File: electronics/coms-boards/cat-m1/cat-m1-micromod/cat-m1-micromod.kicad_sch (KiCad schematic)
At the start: 61 parts

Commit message: removed 3.3v to 1.8v reg from sara-m410m board and approved for pcb routing, added m.2 connector pcb for pycom boards under duel communications board
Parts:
- removed C? (x2): 1uF, symbol Device:C
- removed R?: 100K, symbol Device:R
- removed U?: AP7331-18WG-7, SOT95P285X145-5N, symbol AP7331-18WG-7:AP7331-18WG-7
- added TP?: VCC, symbol Connector:TestPoint
- R?: value 35K -> 10K
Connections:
- net VCC: now also TP?.1
- net GPIO_VCC_ON renamed GPIO_VCC_EN
- net GPIO_V_INT: no longer names the net of J?.57 (F5)
- no-connect marks 34 -> 62
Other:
- note added: "6th October 2022"
- note added: "CAT-M1 M.2 Card"
- note added: "LED Network Indicator"
- note added: "Level Shifter 3.3 V -> 1.8 V"
- note added: "MicroMod Connector"
- note added: "Nano Sim Connector"
- note added: "Reset Switch"
- note added: "USB-C Connector"
- note removed: "1.8 V Reference Voltage"
- note removed: "MQTT"
- note removed: "Note. EN1V8 should be pulled low before GPIO_VCC_ON is switched off."
- moved on the sheet: C?, D?, J?, L?, Q?, R?, U?

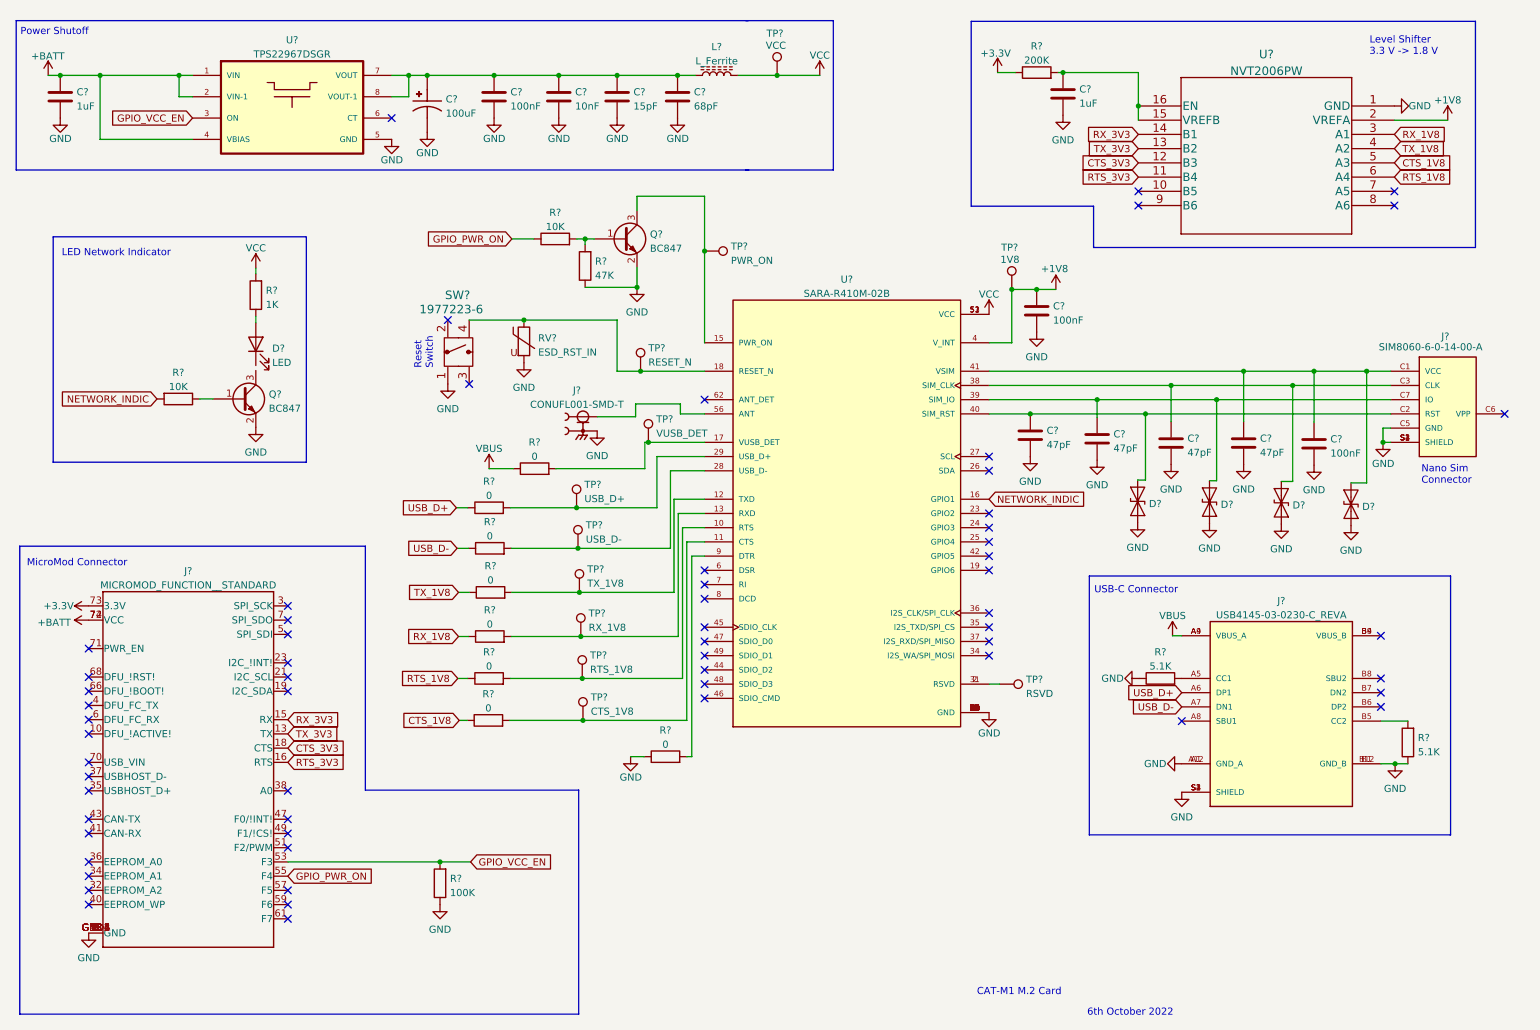
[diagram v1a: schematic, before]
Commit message: finalised cat-m1 m.2 connector board for communications
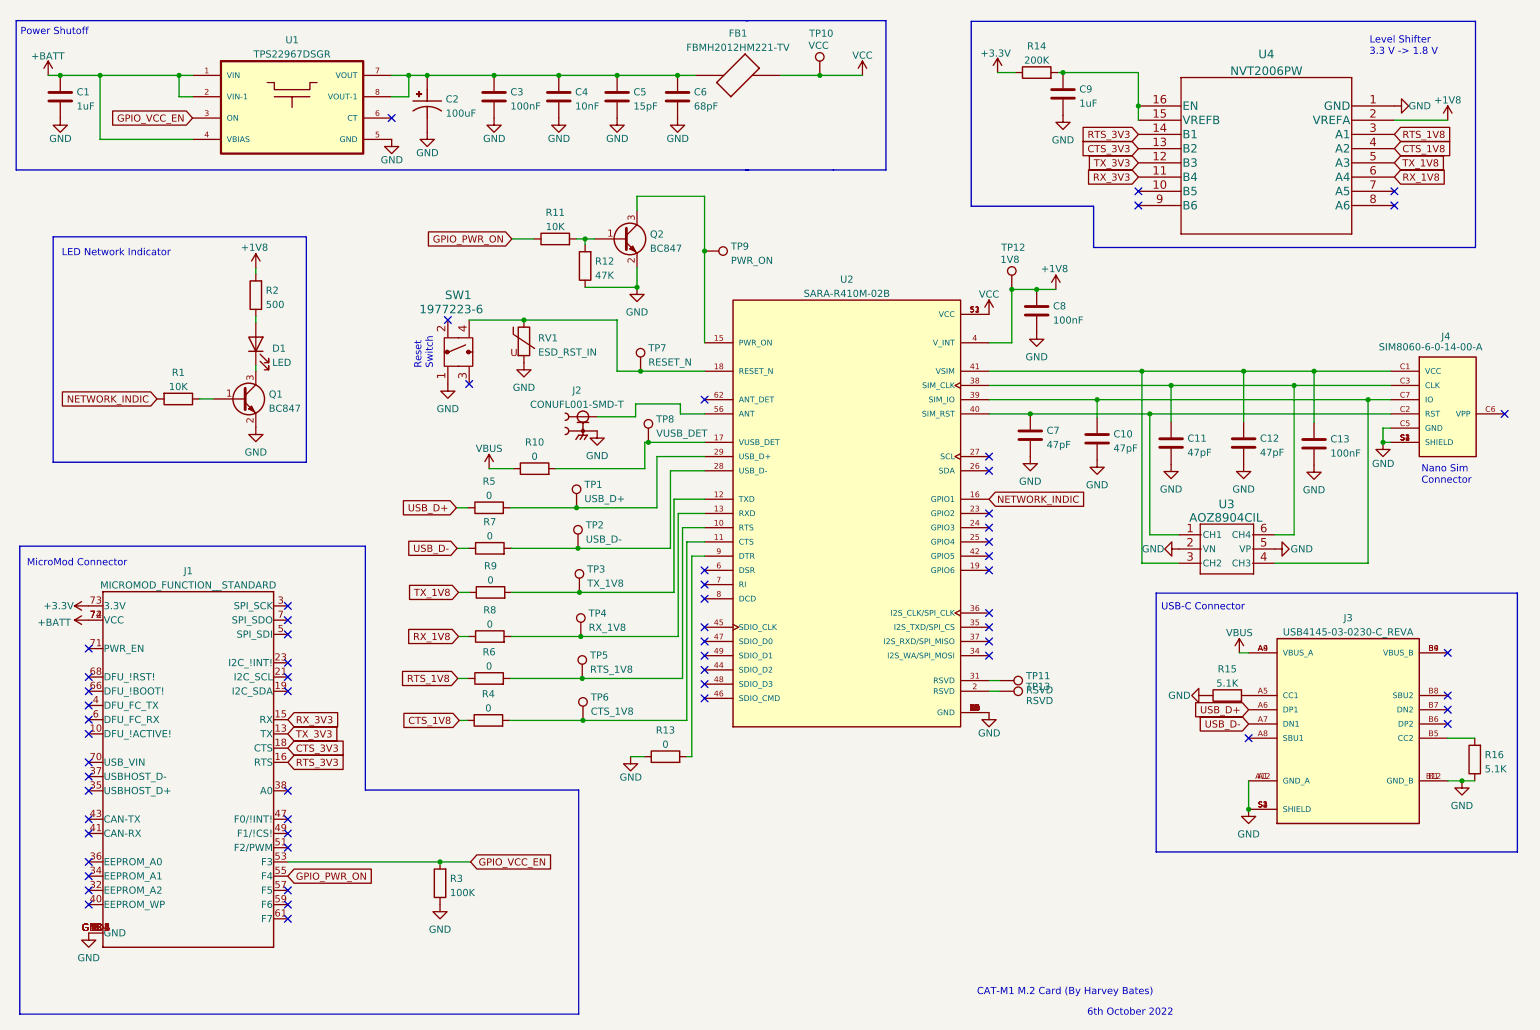
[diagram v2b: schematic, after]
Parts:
- removed D? (x4): PESD0402-140, symbol Diode:SD05_SOD323
- removed L?: L_Ferrite, symbol Device:L_Ferrite
- added FB1: FBMH2012HM221-TV, FBMH2012HM221-TV:BEADC2012X105N, symbol FBMH2012HM221-TV:FBMH2012HM221-TV
- added TP13: RSVD, TestPoint:TestPoint_Pad_D1.0mm, symbol Connector:TestPoint
- added U3: AOZ8904CIL, AOZ8904CIL:AOZ8904CIL, symbol AOZ8904CIL:AOZ8904CIL
- C1, C10, C11, C12, C13, C3, C4, C5, C6, C7, C8, C9: renamed from C?; footprint (none) -> Capacitor_SMD:C_0805_2012Metric
- C2: renamed from C?; footprint CAPPM3528X210N -> T520B107M006ATE015:CAPPM3528X210N
- D1: renamed from D?; footprint (none) -> Capacitor_SMD:C_0805_2012Metric
- J2: renamed from J?; footprint LINX_CONUFL001-SMD-T -> CONUFL001-SMD-T:LINX_CONUFL001-SMD-T
- J3: renamed from J?; footprint GCT_USB4145-03-0230-C_REVA -> USB4145-03-0230-C_REVA:GCT_USB4145-03-0230-C_REVA
- J4: renamed from J?; footprint GCT_SIM8060-6-0-14-00-A -> SIM8060-6-0-14-00-A:GCT_SIM8060-6-0-14-00-A
- R1, R10, R11, R12, R13, R14, R15, R16, R3, R4, R5, R6, R7, R8, R9: renamed from R?; footprint (none) -> Resistor_SMD:R_0805_2012Metric
- R2: renamed from R?; value 1K -> 500; footprint (none) -> Resistor_SMD:R_0805_2012Metric
- RV1: renamed from RV?; footprint (none) -> Resistor_SMD:R_0805_2012Metric; Component (none) -> VC080518A400DP
- SW1: renamed from SW?; footprint SW_1977223-6_TEC -> footprints:1977223-6
- TP1, TP10, TP11, TP12, TP2, TP3, TP4, TP5, TP6, TP7, TP8, TP9: renamed from TP?; footprint (none) -> TestPoint:TestPoint_Pad_D1.0mm
- U1: renamed from U?; footprint SON50P200X200X80-9N -> TPS22967DSGR:SON50P200X200X80-9N
- U2: renamed from U?; footprint XCVR_SARA-R410M-02B -> SARA-R410M-02B:XCVR_SARA-R410M-02B
- U4: renamed from U?; footprint TSSOP16_SOT403-1_NXP -> NVT2006PW:NVT2006PW
- gave numbers to parts that had none: 3
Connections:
- net +1V8: now also R2.2
- net CTS_1V8: now also U4.4 (A2); no longer U4.5 (A3)
- net CTS_3V3: now also U4.13 (B2); no longer U4.12 (B3)
- net GND: now also U3.2 (VN), U3.5 (VP)
- net RTS_1V8: now also U4.3 (A1); no longer U4.6 (A4)
- net RTS_3V3: now also U4.14 (B1); no longer U4.11 (B4)
- net RX_1V8: now also U4.6 (A4); no longer U4.3 (A1)
- net RX_3V3: now also U4.11 (B4); no longer U4.14 (B1)
- net TX_1V8: now also U4.5 (A3); no longer U4.4 (A2)
- net TX_3V3: now also U4.12 (B3); no longer U4.13 (B2)
- net VCC: now also FB1.2; no longer R2.2
- net at C12.1, C13.1, J4.C1 (VCC)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: now also U3.3 (CH2)
- net at C7.1, J4.C2 (RST), U2.40 (SIM_RST): now also U3.1 (CH1)
- net at C11.1, J4.C3 (CLK), U2.38 (SIM_CLK): now also U3.6 (CH4)
- net at C10.1, J4.C7 (IO), U2.39 (SIM_IO): now also U3.4 (CH3)
- net at Q1.3 (C): now also D1.1 (K)
- net at C2.1, C3.1, C4.1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: now also FB1.1
- net at TP11.1, U2.31 (RSVD): no longer U2.2 (RSVD)
- new net: TP13.1, U2.2 (RSVD)
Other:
- note added: "CAT-M1 M.2 Card (By Harvey Bates)"
- note removed: "CAT-M1 M.2 Card"
- moved on the sheet: J3, R15, R16, TP10, TP11

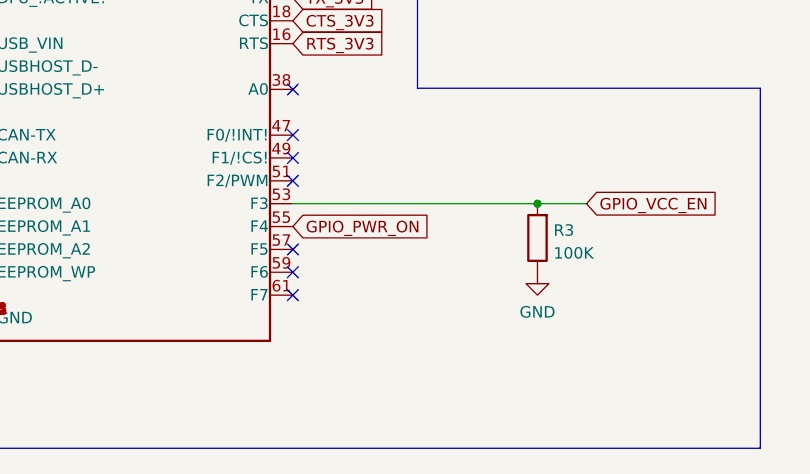
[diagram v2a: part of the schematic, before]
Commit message: updated to re-align with master
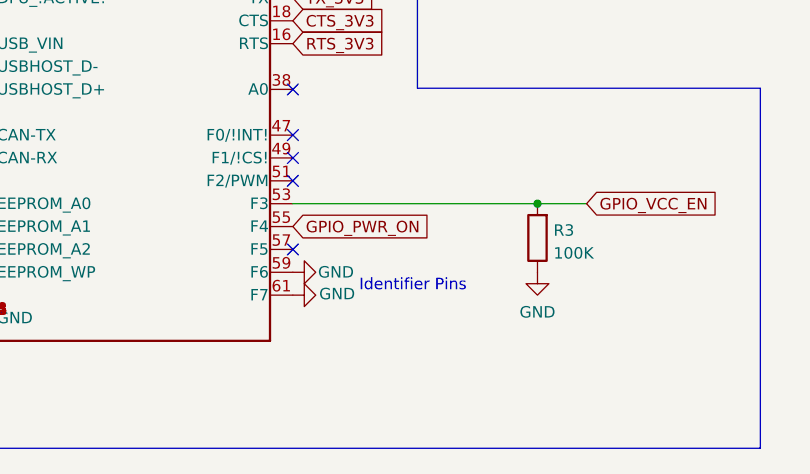
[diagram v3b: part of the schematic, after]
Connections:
- net GND: now also J1.59 (F6), J1.61 (F7)
- no-connect marks 62 -> 60
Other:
- note added: "Identifier Pins"
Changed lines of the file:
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@@
   (no_connect (at 28.321 133.604))
   (no_connect (at 63.881 161.544))
-  (no_connect (at 63.881 176.784))
   (no_connect (at 63.881 164.084))
   (no_connect (at 63.881 159.004))
@@
   (no_connect (at 189.103 129.794))
   (no_connect (at 281.178 86.614))
-  (no_connect (at 63.881 174.244))
   (no_connect (at 63.881 171.704))
   (no_connect (at 189.103 96.774))
@@
     (effects (font (size 1.27 1.27)) (justify left bottom))
   )
+  (text "Identifier Pins" (at 71.247 176.53 0)
+    (effects (font (size 1.27 1.27)) (justify left bottom))
+  )
   (text "USB-C Connector" (at 219.837 121.92 0)
     (effects (font (size 1.27 1.27)) (justify left bottom))
@@
     )
     (property "Datasheet" "~" (id 3) (at 121.285 126.365 0)
+      (effects (font (size 1.27 1.27)) hide)
+    )
+    (pin "1")
+  )
+  (symbol (lib_id "power:GND") (at 63.881 174.244 90) (unit 1)
+    (in_bom yes) (on_board yes)
+    (property "Reference" "#PWR?" (id 0) (at 70.231 174.244 0)
+      (effects (font (size 1.27 1.27)) hide)
+    )
+    (property "Value" "GND" (id 1) (at 66.675 174.244 90)
+      (effects (font (size 1.27 1.27)) (justify right))
+    )
+    (property "Footprint" "" (id 2) (at 63.881 174.244 0)
+      (effects (font (size 1.27 1.27)) hide)
+    )
+    (property "Datasheet" "" (id 3) (at 63.881 174.244 0)
       (effects (font (size 1.27 1.27)) hide)
     )
@@
     (pin "1")
   )
+  (symbol (lib_id "power:GND") (at 63.881 176.784 90) (unit 1)
+    (in_bom yes) (on_board yes)
+    (property "Reference" "#PWR?" (id 0) (at 70.231 176.784 0)
+      (effects (font (size 1.27 1.27)) hide)
+    )
+    (property "Value" "GND" (id 1) (at 66.802 176.657 90)
+      (effects (font (size 1.27 1.27)) (justify right))
+    )
+    (property "Footprint" "" (id 2) (at 63.881 176.784 0)
+      (effects (font (size 1.27 1.27)) hide)
+    )
+    (property "Datasheet" "" (id 3) (at 63.881 176.784 0)
+      (effects (font (size 1.27 1.27)) hide)
+    )
+    (pin "1")
+  )
   (symbol (lib_id "Connector:TestPoint") (at 128.27 91.694 0) (unit 1)
     (in_bom yes) (on_board yes) (fields_autoplaced)
@@
       (reference "#PWR0101") (unit 1) (value "+1V8") (footprint "")
     )
+    (path "/0eaa0237-d502-45ee-9f1b-9a5fa7a28cc0"
+      (reference "#PWR?") (unit 1) (value "GND") (footprint "")
+    )
+    (path "/3e0b8633-be28-4a44-a159-8f3ca70c589b"
+      (reference "#PWR?") (unit 1) (value "GND") (footprint "")
+    )
     (path "/e4b3f069-5800-42de-af54-8d884a9881b4"

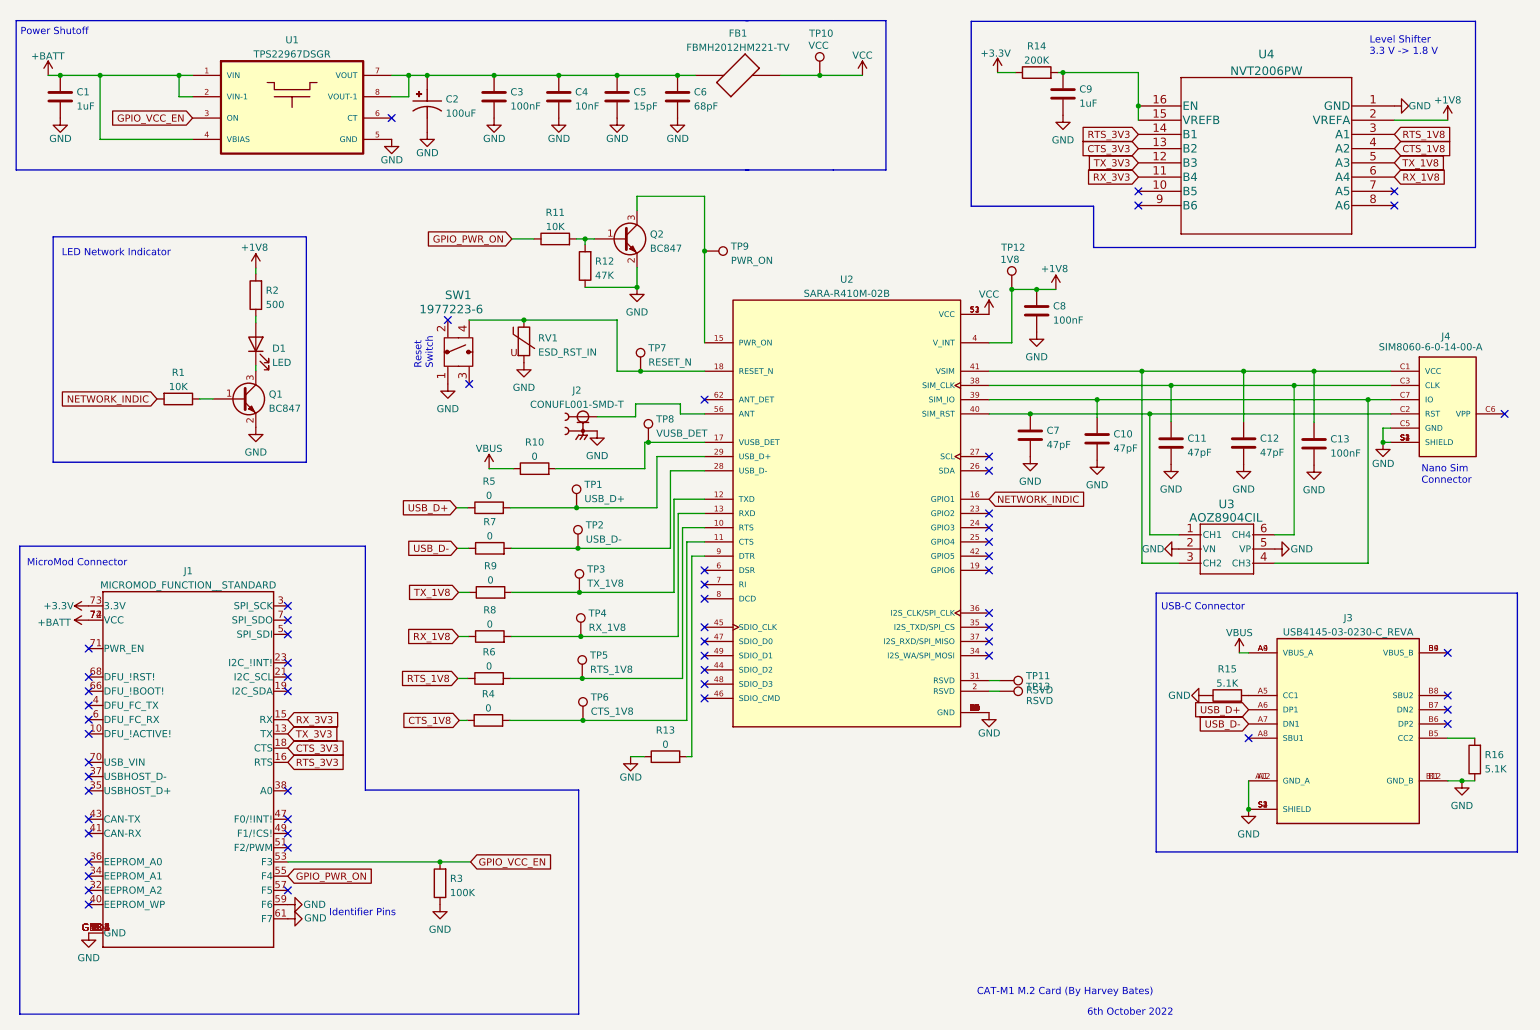
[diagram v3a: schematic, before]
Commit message: realign with master branch before kangaroo board is split into seperate repo
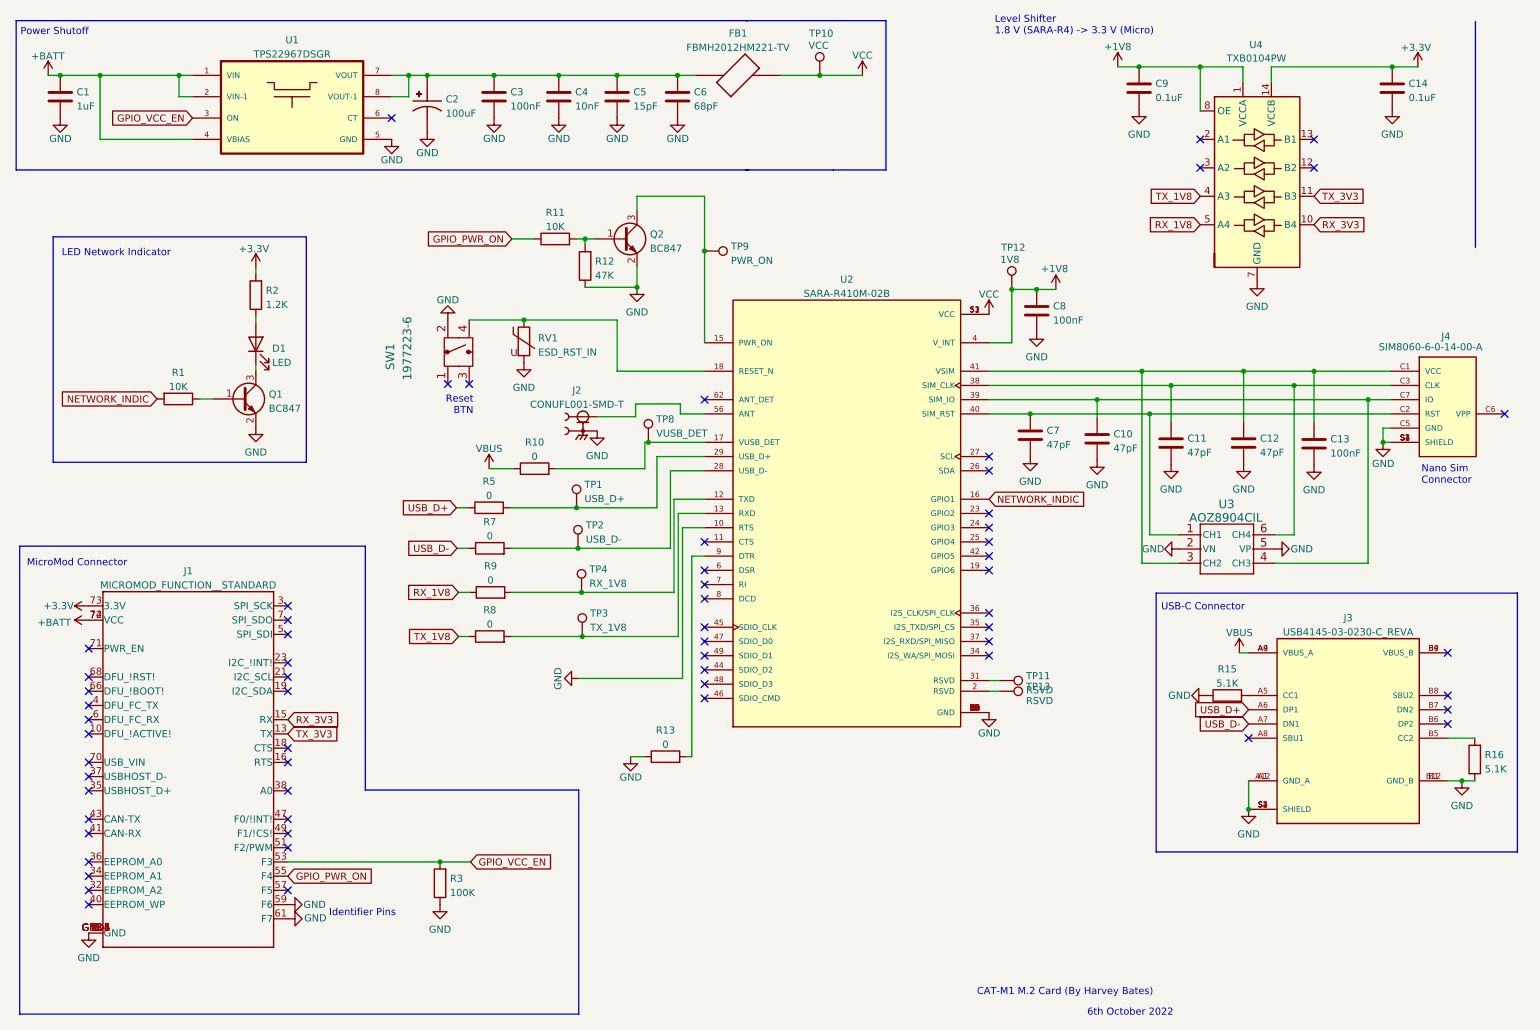
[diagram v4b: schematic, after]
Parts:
- removed R14: 200K, Resistor_SMD:R_0805_2012Metric, symbol Device:R
- removed R4, R6: 0, Resistor_SMD:R_0805_2012Metric, symbol Device:R
- removed TP5: RTS_1V8, TestPoint:TestPoint_Pad_D1.0mm, symbol Connector:TestPoint
- removed TP6: CTS_1V8, TestPoint:TestPoint_Pad_D1.0mm, symbol Connector:TestPoint
- removed TP7: RESET_N, TestPoint:TestPoint_Pad_D1.0mm, symbol Connector:TestPoint
- removed U4: NVT2006PW, NVT2006PW:NVT2006PW, symbol NVT2006PW:NVT2006PW
- added C14: 0.1uF, Capacitor_SMD:C_0805_2012Metric, symbol Device:C
- added U4: TXB0104PW, Package_SO:TSSOP-14_4.4x5mm_P0.65mm, symbol Logic_LevelTranslator:TXB0104PW
- C9: value 1uF -> 0.1uF
- R2: value 500 -> 1.2K
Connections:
- net +1V8: now also C9.1, U4.1 (VCCA), U4.8 (OE); no longer R2.2
- net +3.3V: now also R2.2, C14.1, U4.14 (VCCB)
- net GND: now also SW1.2, U2.10 (RTS), C14.2, U4.7 (GND); no longer SW1.1
- net RX_1V8: now also R9.1, U4.5 (A4); no longer R8.1
- net RX_3V3: now also U4.10 (B4)
- net TX_1V8: now also R8.1, U4.4 (A3); no longer R9.1
- net TX_3V3: now also U4.11 (B3)
- net at R8.2, U2.13 (RXD): now also TP3.1; no longer TP4.1
- net at R9.2, U2.12 (TXD): now also TP4.1; no longer TP3.1
- net CTS_3V3: no longer names the net of J1.18 (CTS)
- net RTS_3V3: no longer names the net of J1.16 (RTS)
- no-connect marks 60 -> 63
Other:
- note added: "Level Shifter 1.8 V (SARA-R4) -> 3.3 V (Micro)"
- note added: "Reset BTN"
- note removed: "Level Shifter 3.3 V -> 1.8 V"
- note removed: "Reset Switch"
- moved on the sheet: C9, TP3, TP4
